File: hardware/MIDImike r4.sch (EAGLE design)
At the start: 8 parts, among them SW1 PUSH-BTN, SW2 SH-7030TB

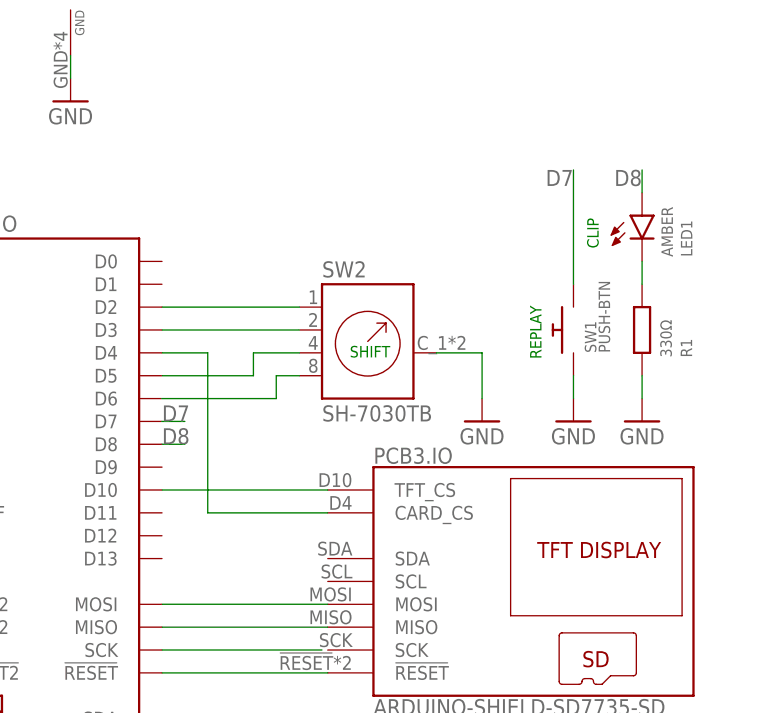
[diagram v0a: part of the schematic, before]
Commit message: rm replay btn; mv clip led to D7
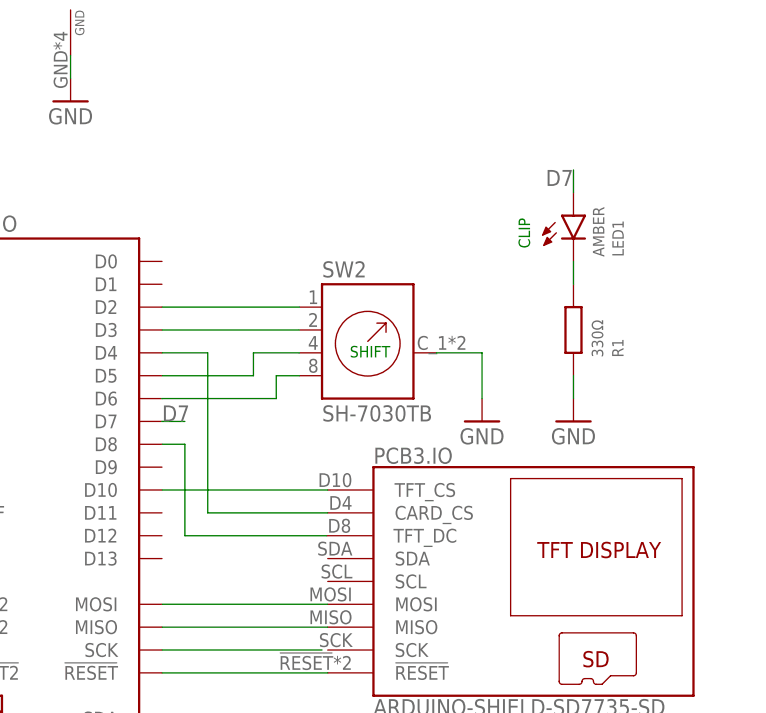
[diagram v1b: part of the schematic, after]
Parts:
- removed SW1: PUSH-BTN, Coert-Vonk:PUSH-BTN
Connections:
- removed net D8: LED1.A, PCB2.IO.D8
- new net N$11: PCB2.IO.D8, PCB3.IO.TFT_DC
- net D7: now also LED1.A; no longer SW1.2
- net GND: no longer SW1.1
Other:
- note removed: "REPLAY"
- moved on the sheet: LED1, R1
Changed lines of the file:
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@@
 <part name="GND2" library="Coert-Vonk" deviceset="GND" device=""/>
 <part name="GND3" library="Coert-Vonk" deviceset="GND" device=""/>
-<part name="SW1" library="Coert-Vonk" deviceset="PUSH-BTN" device=""/>
 <part name="GND5" library="Coert-Vonk" deviceset="GND" device=""/>
 <part name="GND6" library="Coert-Vonk" deviceset="GND" device=""/>
@@
 <part name="LED1" library="OPNpool" deviceset="LED" device="CHIPLED_0805" package3d_urn="urn:adsk.eagle:package:15821/2" value="AMBER"/>
 <part name="GND4" library="Coert-Vonk" deviceset="GND" device=""/>
-<part name="GND7" library="Coert-Vonk" deviceset="GND" device=""/>
 <part name="GND8" library="Coert-Vonk" deviceset="GND" device=""/>
 <part name="SW2" library="Coert-Vonk" deviceset="SH-7030TB" device=""/>
@@
 <plain>
 <text x="40.64" y="88.9" size="1.778" layer="91" align="bottom-center">USB-MIDI</text>
-<text x="125.984" y="111.506" size="1.27" layer="91" rot="R90" align="bottom-center">REPLAY</text>
 <text x="55.88" y="66.04" size="1.778" layer="91" align="bottom-right">USB-MIDI or USB-SERIAL</text>
-<text x="132.334" y="124.206" size="1.27" layer="91" rot="R90" align="bottom-right">CLIP</text>
+<text x="124.714" y="124.206" size="1.27" layer="91" rot="R90" align="bottom-right">CLIP</text>
 <text x="106.934" y="109.982" size="1.27" layer="91" rot="R180" align="bottom-center">SHIFT</text>
 </plain>
@@
 <attribute name="VALUE" x="60.96" y="134.62" size="1.778" layer="96" align="bottom-center"/>
 </instance>
-<instance part="SW1" gate="G$1" x="129.54" y="111.76" smashed="yes" rot="R90">
-<attribute name="NAME" x="132.07618125" y="109.218090625" size="1.27" layer="95" rot="R90"/>
-<attribute name="VALUE" x="133.607609375" y="109.218190625" size="1.27" layer="96" rot="R90"/>
-</instance>
 <instance part="GND5" gate="1" x="40.64" y="76.2" smashed="yes">
 <attribute name="VALUE" x="40.64" y="73.66" size="1.778" layer="96" align="bottom-center"/>
 </instance>
-<instance part="GND6" gate="1" x="137.16" y="101.6" smashed="yes">
-<attribute name="VALUE" x="137.16" y="99.06" size="1.778" layer="96" align="bottom-center"/>
+<instance part="GND6" gate="1" x="129.54" y="101.6" smashed="yes">
+<attribute name="VALUE" x="129.54" y="99.06" size="1.778" layer="96" align="bottom-center"/>
 </instance>
 <instance part="PCB1" gate=".IO" x="27.94" y="111.76" smashed="yes">
@@
 <attribute name="VALUE" x="46.355" y="83.82" size="1.778" layer="96" rot="R90"/>
 </instance>
-<instance part="R1" gate="G$1" x="137.16" y="111.76" smashed="yes" rot="MR90">
-<attribute name="MANF" x="137.16" y="111.76" size="1.778" layer="96" rot="MR90" display="off"/>
-<attribute name="MANF#" x="137.16" y="111.76" size="1.778" layer="96" rot="MR90" display="off"/>
-<attribute name="MOUSER#" x="137.16" y="111.76" size="1.778" layer="96" rot="MR90" display="off"/>
-<attribute name="NAME" x="141.4526" y="108.712" size="1.27" layer="95" rot="MR90"/>
-<attribute name="VALUE" x="139.192" y="108.712" size="1.27" layer="96" rot="MR90"/>
-</instance>
-<instance part="LED1" gate="G$1" x="137.16" y="124.46" smashed="yes">
-<attribute name="NAME" x="142.748" y="119.888" size="1.27" layer="95" rot="R90"/>
-<attribute name="VALUE" x="140.589" y="119.888" size="1.27" layer="96" rot="R90"/>
+<instance part="R1" gate="G$1" x="129.54" y="111.76" smashed="yes" rot="MR90">
+<attribute name="MANF" x="129.54" y="111.76" size="1.778" layer="96" rot="MR90" display="off"/>
+<attribute name="MANF#" x="129.54" y="111.76" size="1.778" layer="96" rot="MR90" display="off"/>
+<attribute name="MOUSER#" x="129.54" y="111.76" size="1.778" layer="96" rot="MR90" display="off"/>
+<attribute name="NAME" x="133.8326" y="108.712" size="1.27" layer="95" rot="MR90"/>
+<attribute name="VALUE" x="131.572" y="108.712" size="1.27" layer="96" rot="MR90"/>
+</instance>
+<instance part="LED1" gate="G$1" x="129.54" y="124.46" smashed="yes">
+<attribute name="NAME" x="135.128" y="119.888" size="1.27" layer="95" rot="R90"/>
+<attribute name="VALUE" x="132.969" y="119.888" size="1.27" layer="96" rot="R90"/>
 </instance>
 <instance part="GND4" gate="1" x="45.72" y="104.14" smashed="yes">
 <attribute name="VALUE" x="45.72" y="101.6" size="1.778" layer="96" align="bottom-center"/>
-</instance>
-<instance part="GND7" gate="1" x="129.54" y="101.6" smashed="yes">
-<attribute name="VALUE" x="129.54" y="99.06" size="1.778" layer="96" align="bottom-center"/>
 </instance>
 <instance part="GND8" gate="1" x="119.38" y="101.6" smashed="yes">
@@
 <pinref part="GND6" gate="1" pin="GND"/>
 <pinref part="R1" gate="G$1" pin="1"/>
-<wire x1="137.16" y1="106.68" x2="137.16" y2="104.14" width="0.1524" layer="91"/>
+<wire x1="129.54" y1="106.68" x2="129.54" y2="104.14" width="0.1524" layer="91"/>
 </segment>
 <segment>
@@
 <pinref part="GND4" gate="1" pin="GND"/>
 <wire x1="45.72" y1="116.84" x2="45.72" y2="106.68" width="0.1524" layer="91"/>
-</segment>
-<segment>
-<wire x1="129.54" y1="106.68" x2="129.54" y2="104.14" width="0.1524" layer="91"/>
-<pinref part="SW1" gate="G$1" pin="1"/>
-<pinref part="GND7" gate="1" pin="GND"/>
 </segment>
 <segment>
@@
 <pinref part="LED1" gate="G$1" pin="C"/>
 <pinref part="R1" gate="G$1" pin="2"/>
-<wire x1="137.16" y1="119.38" x2="137.16" y2="116.84" width="0.1524" layer="91"/>
-</segment>
-</net>
-<net name="D8" class="0">
-<segment>
-<pinref part="LED1" gate="G$1" pin="A"/>
-<wire x1="137.16" y1="127" x2="137.16" y2="129.54" width="0.1524" layer="91"/>
-<label x="137.16" y="129.54" size="1.778" layer="95" rot="R180"/>
-</segment>
-<segment>
-<pinref part="PCB2" gate=".IO" pin="D8"/>
-<wire x1="83.82" y1="99.06" x2="86.36" y2="99.06" width="0.1524" layer="91"/>
-<label x="83.82" y="99.06" size="1.778" layer="95"/>
+<wire x1="129.54" y1="119.38" x2="129.54" y2="116.84" width="0.1524" layer="91"/>
 </segment>
 </net>
@@
 </segment>
 <segment>
-<pinref part="SW1" gate="G$1" pin="2"/>
-<wire x1="129.54" y1="116.84" x2="129.54" y2="129.54" width="0.1524" layer="91"/>
+<pinref part="LED1" gate="G$1" pin="A"/>
+<wire x1="129.54" y1="127" x2="129.54" y2="129.54" width="0.1524" layer="91"/>
 <label x="129.54" y="129.54" size="1.778" layer="95" rot="R180"/>
 </segment>
@@
 </segment>
 </net>
+<net name="N$11" class="0">
+<segment>
+<pinref part="PCB2" gate=".IO" pin="D8"/>
+<wire x1="83.82" y1="99.06" x2="86.36" y2="99.06" width="0.1524" layer="91"/>
+<wire x1="86.36" y1="99.06" x2="86.36" y2="88.9" width="0.1524" layer="91"/>
+<pinref part="PCB3" gate=".IO" pin="TFT_DC"/>
+<wire x1="86.36" y1="88.9" x2="102.108" y2="88.9" width="0.1524" layer="91"/>
+</segment>
+</net>
